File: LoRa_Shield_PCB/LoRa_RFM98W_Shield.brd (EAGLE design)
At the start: 53.6 x 59.9 mm, 40 parts, among them IC1 AHT10, IC2 TXS0102DCUR, J1 CON_TERMINAL_BLOCK_03-5MM, J2 TYPE-C-31-M-17, U1 RFM98W, U2 3V3_REG, X2 BU-SMA-H

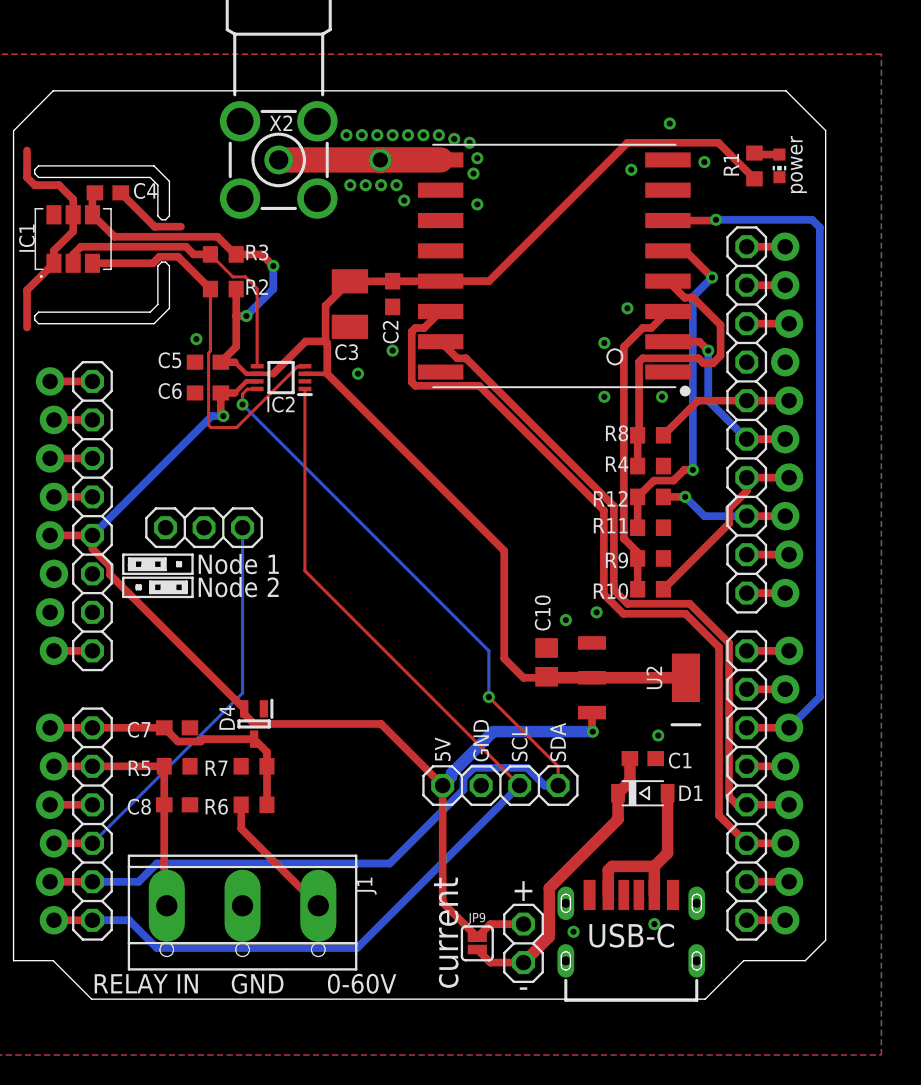
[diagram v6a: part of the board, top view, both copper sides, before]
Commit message: RF feed line impedance fix, added version text
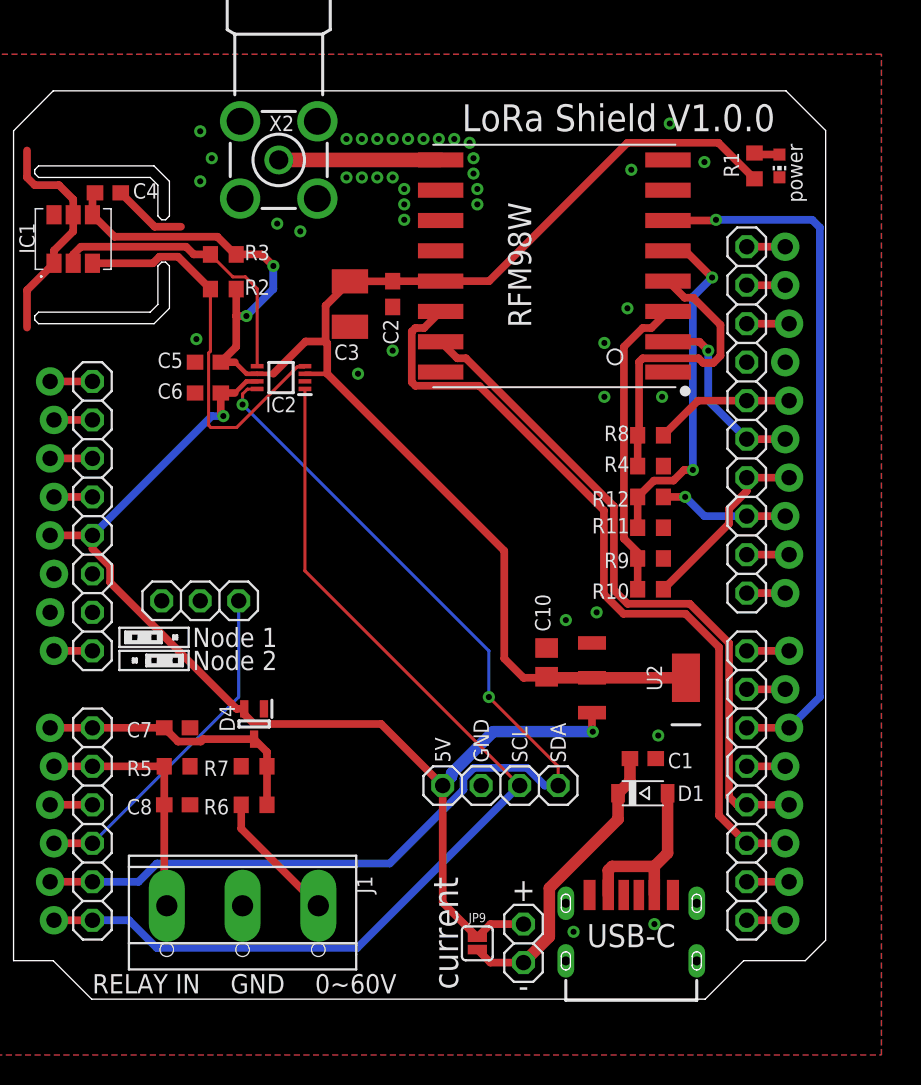
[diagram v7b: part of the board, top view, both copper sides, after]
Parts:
- moved JP6 4.83 mm to (16.0, 30.0)
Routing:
- net N$30: track 27.5 -> 22.5 mm
- net N$2: vias 1 -> 0
- net GND: vias 32 -> 40
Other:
- board text added: "0~60V"
- board text added: "LoRa Shield V1.0.0"
- board text added: "RFM98W"
- board text removed: "0-60V"

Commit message: output files updated
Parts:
- removed C10: 22uF, rcl:C0805
- removed JP9: JUMPER-SMT_2_NC_PASTE_SILK, SparkFun-Jumpers:SMT-JUMPER_2_NC_PASTE_SILK
- added C9: 100nF, rcl:C0603
- added JP7: (no value), pinhead_v2:1X08/OCT
- C2: value 100nF -> 22uF; device rcl:C0603 -> rcl:C0805
- C3: value 100uF -> 100nF; device rcl:SMC_B -> rcl:C0603
- C8: value 100nF -> 100uF; device rcl:C0603 -> rcl:SMC_B
- J1: value CON_TERMINAL_BLOCK_03-5MM -> TYPE-C-31-M-17; device dp_devices:TERMINAL_BLOCK_3P_5 -> angrypig7_Library:TYPE-C-31-M-17
- J2: value TYPE-C-31-M-17 -> CON_TERMINAL_BLOCK_03-5MM; device angrypig7_Library:TYPE-C-31-M-17 -> dp_devices:TERMINAL_BLOCK_3P_5
- JP1: value (none) -> JUMPER-SMT_2_NC_PASTE_SILK; device pinhead_v2:1X08/OCT -> SparkFun-Jumpers:SMT-JUMPER_2_NC_PASTE_SILK
- JP2: value (none) -> current measurement; device pinhead_v2:1X10/OCT -> pinhead_v2:1X02/OCT
- JP3: value (none) -> OLED; device pinhead_v2:1X08/OCT -> pinhead_v2:1X04/OCT
- JP4: device pinhead_v2:1X06/OCT -> pinhead_v2:1X08/OCT
- JP5: value OLED -> (none); device pinhead_v2:1X04/OCT -> pinhead_v2:1X10/OCT
- JP6: value node number -> (none); device pinhead_v2:1X03/OCT -> pinhead_v2:1X06/OCT
- JP8: value current measurement -> node number; device pinhead_v2:1X02/OCT -> pinhead_v2:1X03/OCT
- R10, R12, R8: value 5k -> 10k
- R11, R9: value 10k -> 5k
- R2: value 10k -> 165k
- R4: value 10k -> 15k
- R6: value 165k -> 10k
- R7: value 15k -> 5k
- U1: value RFM98W -> 3V3_REG; device SparkFun-RF:RFM95/96/97/98W -> SamacSys_Parts:SOT230P700X170-4N
- U2: value 3V3_REG -> RFM98W; device SamacSys_Parts:SOT230P700X170-4N -> SparkFun-RF:RFM95/96/97/98W
- moved C4 40.6 mm to (14.5, 16.5)
- moved JP2 37.6 mm to (37.3, 7.37)
- moved C8 35.0 mm to (25.9, 49.6), turned to 270 degrees
- moved R2 34.1 mm to (19.6, 16.5), turned to 180 degrees
- moved R6 34.1 mm to (17.5, 50.5), turned to 0 degrees
- moved R3 33.9 mm to (14.5, 19.1), turned to 180 degrees
- moved R5 33.9 mm to (17.5, 52.8), turned to 0 degrees
- moved R4 32.8 mm to (19.6, 19.1)
- moved JP3 32.3 mm to (35.8, 17.8), turned to 0 degrees
- moved R7 31.6 mm to (45.7, 36.8), turned to 180 degrees
- moved JP8 31.1 mm to (16.0, 30.0), turned to 0 degrees
- moved C3 30.2 mm to (14.5, 21.6), turned to 0 degrees
- moved JP5 29.1 mm to (52.1, 41.9), turned to 270 degrees
- moved U1 27.7 mm to (45.0, 24.9)
- moved U2 27.7 mm to (39.4, 52.1)
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- renumbered B2 to B1, D4 to D2, X2 to X1
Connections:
- net 3.3V: now also C2.2, C5.2, C7.1, C8.+, C9.1, R5.2, R6.2, U1.2, U1.4, U2.3.3V; no longer C10.2, C2.1, C3.+, C4.2, C5.1, R2.2, R3.2, U1.3.3V, U2.2, U2.4
- net 5V: now also JP1.2, JP2.1, JP3.1, JP4.4, U1.3; no longer JP3.4, JP5.1, JP8.1, JP9.2, U2.3
- net GND: now also C2.1, C3.2, C5.1, C8.-, C9.2, J1.GND, J1.GND_2, J1.P$1, J1.P$2, J1.P$3, J1.P$4, J2.2, JP4.2, JP4.3, JP5.4, JP8.1, JP8.2, R10.2, R12.2, R3.1, R4.1, R8.2, U1.1, U2.GND@1, U2.GND@2, U2.GND@3; no longer C10.1, C2.2, C3.-, C5.2, C8.1, J1.2, J2.GND, J2.GND_2, J2.P$1, J2.P$2, J2.P$3, J2.P$4, JP2.4, JP3.3, JP5.2, JP6.1, JP6.2, R11.2, R4.2, R5.1, R7.1, R9.2, U1.GND@1, U1.GND@2, U1.GND@3, U2.1
- net I2C_SCL_3V3: now also R6.1; no longer R2.1
- net I2C_SCL_5V: now also JP3.3, JP6.1; no longer JP4.1, JP5.3
- net I2C_SDA_3V3: now also R5.1; no longer R3.1
- net I2C_SDA_5V: now also JP3.4, JP6.2; no longer JP4.2, JP5.4
- net INPUT_RELAY_STATUS: now also C4.2, J2.1, JP6.5, R3.2; no longer C8.2, J1.1, JP4.5, R5.2
- net INPUT_VOLTAGE_READING: now also C3.1, JP6.6, R2.1, R4.2; no longer C7.1, JP4.6, R6.1, R7.2
- net N$1: now also J1.VBUS, J1.VBUS_2; no longer J2.VBUS, J2.VBUS_2
- net N$10: now also JP7.4; no longer JP1.4
- net N$12: now also JP5.9; no longer JP2.9
- net N$13: now also JP5.10; no longer JP2.10
- net N$14: now also JP7.1; no longer JP1.1
- net N$15: now also JP7.2; no longer JP1.2
- net N$16: now also JP1.1, JP2.2; no longer JP8.2, JP9.1
- net N$2: now also U2.ANT; no longer U1.ANT
- net N$20: now also JP7.7; no longer JP1.7
- net N$21: now also JP7.8; no longer JP1.8
- net N$23: now also JP4.5; no longer JP3.5
- net N$24: now also JP4.6; no longer JP3.6
- net N$25: now also JP4.7; no longer JP3.7
- net N$26: now also JP4.8; no longer JP3.8
- net N$29: now also JP6.4; no longer JP4.4
- net N$3: now also JP5.1; no longer JP2.1
- net N$30: now also JP8.3; no longer JP4.3
- net N$5: now also JP5.2; no longer JP2.2
- net N$6: now also JP5.3; no longer JP2.3
- net N$7: now also JP4.1; no longer JP3.1
- net N$8: now also J2.3, R2.2; no longer J1.3, R6.2
- net RFM_DIO0: now also JP7.6, U2.DIO0; no longer JP1.6, U1.DIO0
- net RFM_DIO1: now also JP7.5, U2.DIO1; no longer JP1.5, U1.DIO1
- net RFM_RESET: now also JP7.3, U2.!RESET; no longer JP1.3, U1.!RESET
- net SPI_CLK_3V3: now also R11.2, R12.1, U2.SCK; no longer R4.1, R8.2, U1.SCK
- net SPI_CLK_5V: now also JP5.5, R11.1; no longer JP2.5, R8.1
- net SPI_MISO: now also JP5.6, U2.MISO; no longer JP2.6, U1.MISO
- net SPI_MOSI_3V3: now also R10.1, R9.2, U2.MOSI; no longer R10.2, R9.1, U1.MOSI
- net SPI_MOSI_5V: now also JP5.7, R9.1; no longer JP2.7, R10.1
- net SPI_SS_RFM_3V3: now also R7.2, R8.1, U2.NSS; no longer R11.1, R12.2, U1.NSS
- net SPI_SS_RFM_5V: now also JP5.8, R7.1; no longer JP2.8, R12.1
